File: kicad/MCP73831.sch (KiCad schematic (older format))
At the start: 13 parts, among them J1 BATT, U2 MCP73831-2-OT

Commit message: improve kicad
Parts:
- added TP1: TestPoint_2Pole, TestPoint:TestPoint_2Pads_Pitch2.54mm_Drill0.8mm, symbol Connector:TestPoint_2Pole
- R6: value 1M -> 270k
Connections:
- net GND: now also TP1.2
- net VOUT: now also TP1.1
- net VBAT: now reaches C2.1, D1.2 (S), J1.2 (Pin_2), R5.1, U2.3 (VBAT)
- net STAT renamed V_STATUS
- net VOLT renamed V_PROBE
- no-connect marks 1 -> 0
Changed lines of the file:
@@
 Text HLabel 4250 2500 0    50   Input ~ 0
 VIN
-Text HLabel 8850 2700 2    50   Input ~ 0
+Text HLabel 8850 2700 2    50   Output ~ 0
 VOUT
 Wire Wire Line
@@
 	6200 3700 6200 3800
 Text HLabel 6100 3350 0    50   Input ~ 0
-STAT
+V_STATUS
 Wire Wire Line
 	6100 3350 6200 3350
@@
 P 7550 3300
 F 0 "R6" H 7620 3346 50  0000 L CNN
-F 1 "1M" H 7620 3255 50  0000 L CNN
+F 1 "270k" H 7620 3255 50  0000 L CNN
 F 2 "Resistor_SMD:R_0805_2012Metric_Pad1.15x1.40mm_HandSolder" V 7480 3300 50  0001 C CNN
 F 3 "~" H 7550 3300 50  0001 C CNN
@@
 	1    0    0    -1
 $EndComp
-Text HLabel 8050 3100 2    50   Input ~ 0
-VOLT
+Text HLabel 8050 3100 2    50   Output ~ 0
+V_PROBE
 Wire Wire Line
 	6100 2700 6650 2700
@@
 $EndComp
 Wire Wire Line
-	6650 2700 7100 2700
+	6650 2700 6850 2700
 Connection ~ 6650 2700
 Wire Wire Line
@@
 	7700 2350 7950 2350
 Connection ~ 7950 2350
-NoConn ~ 7250 2750
+$Comp
+L Connector:TestPoint_2Pole TP1
+U 1 1 5C3B9527
+P 8500 2900
+F 0 "TP1" V 8454 2958 50  0000 L CNN
+F 1 "TestPoint_2Pole" V 8545 2958 50  0000 L CNN
+F 2 "TestPoint:TestPoint_2Pads_Pitch2.54mm_Drill0.8mm" H 8500 2900 50  0001 C CNN
+F 3 "~" H 8500 2900 50  0001 C CNN
+	1    8500 2900
+	0    1    1    0
+$EndComp
+$Comp
+L power:GND #PWR0121
+U 1 1 5C3B95F4
+P 8500 3200
+F 0 "#PWR0121" H 8500 2950 50  0001 C CNN
+F 1 "GND" H 8505 3027 50  0000 C CNN
+F 2 "" H 8500 3200 50  0001 C CNN
+F 3 "" H 8500 3200 50  0001 C CNN
+	1    8500 3200
+	1    0    0    -1
+$EndComp
+Wire Wire Line
+	8500 3100 8500 3200
+Text HLabel 6950 2500 2    50   Output ~ 0
+VBAT
+Wire Wire Line
+	6850 2700 6850 2500
+Wire Wire Line
+	6850 2500 6950 2500
+Connection ~ 6850 2700
+Wire Wire Line
+	6850 2700 7100 2700
 $EndSCHEMATC

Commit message: updates
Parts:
- D1: symbol DMP1045U:DMP1045U -> esp8266-rescue:DMP1045U-DMP1045U
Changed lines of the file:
@@
 $Descr A4 11693 8268
 encoding utf-8
-Sheet 2 3
+Sheet 2 4
 Title ""
 Date ""
@@
 	7100 3000 7100 3150
 $Comp
-L DMP1045U:DMP1045U D1
+L esp8266-rescue:DMP1045U-DMP1045U D1
 U 1 1 5C39EFFF
 P 8050 2700

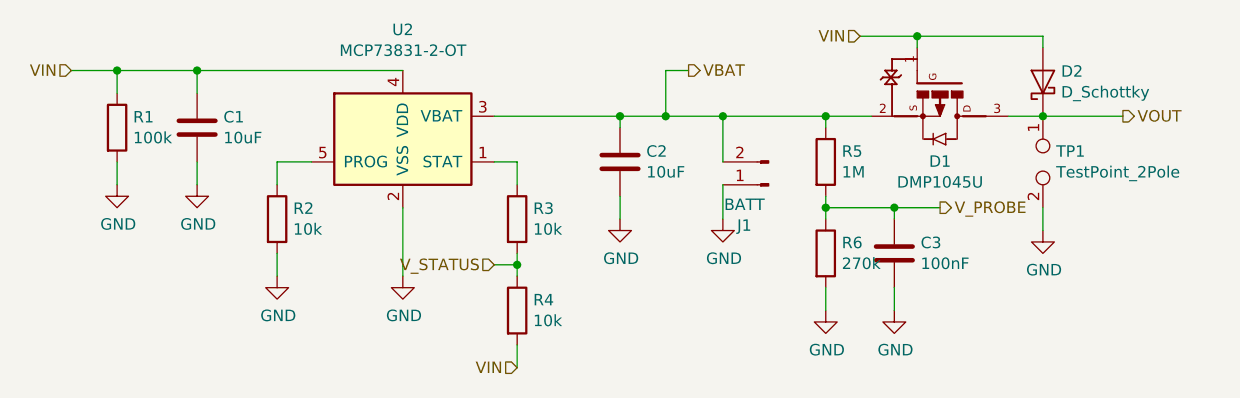
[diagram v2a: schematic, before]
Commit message: add 18B20 on board
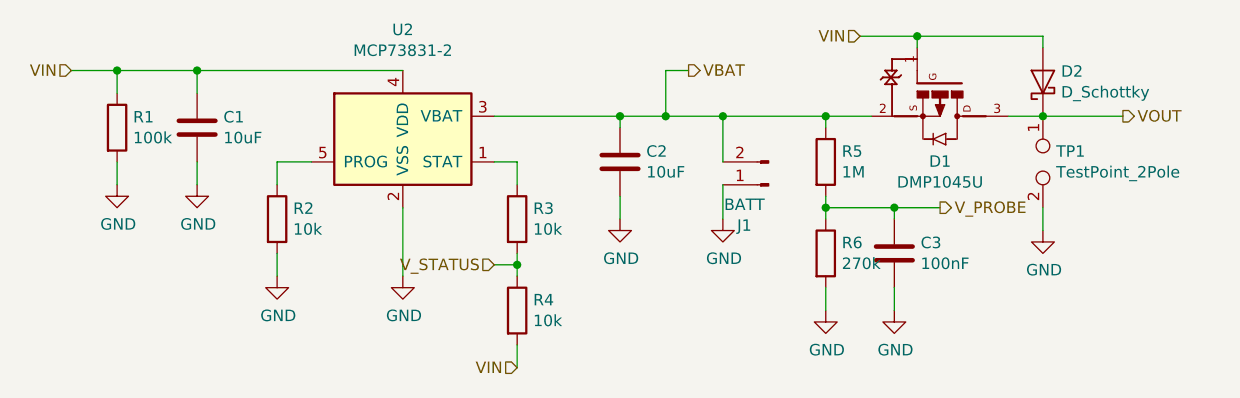
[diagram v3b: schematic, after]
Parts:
- U2: value MCP73831-2-OT -> MCP73831-2
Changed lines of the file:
@@
 P 5700 2800
 F 0 "U2" H 5700 3278 50  0000 C CNN
-F 1 "MCP73831-2-OT" H 5700 3187 50  0000 C CNN
+F 1 "MCP73831-2" H 5700 3187 50  0000 C CNN
 F 2 "Package_TO_SOT_SMD:SOT-23-5" H 5750 2550 50  0001 L CIN
 F 3 "http://ww1.microchip.com/downloads/en/DeviceDoc/20001984g.pdf" H 5550 2750 50  0001 C CNN

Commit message: correst bsp75 footprint
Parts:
- C1: footprint Capacitor_SMD:C_0805_2012Metric_Pad1.15x1.40mm_HandSolder -> Connector_Wire:SolderWirePad_1x01_SMD_5x10mm
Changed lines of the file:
@@
 F 0 "C1" H 4915 2796 50  0000 L CNN
 F 1 "10uF" H 4915 2705 50  0000 L CNN
-F 2 "Capacitor_SMD:C_0805_2012Metric_Pad1.15x1.40mm_HandSolder" H 4838 2600 50  0001 C CNN
+F 2 "Connector_Wire:SolderWirePad_1x01_SMD_5x10mm" H 4838 2600 50  0001 C CNN
 F 3 "~" H 4800 2750 50  0001 C CNN
 	1    4800 2750

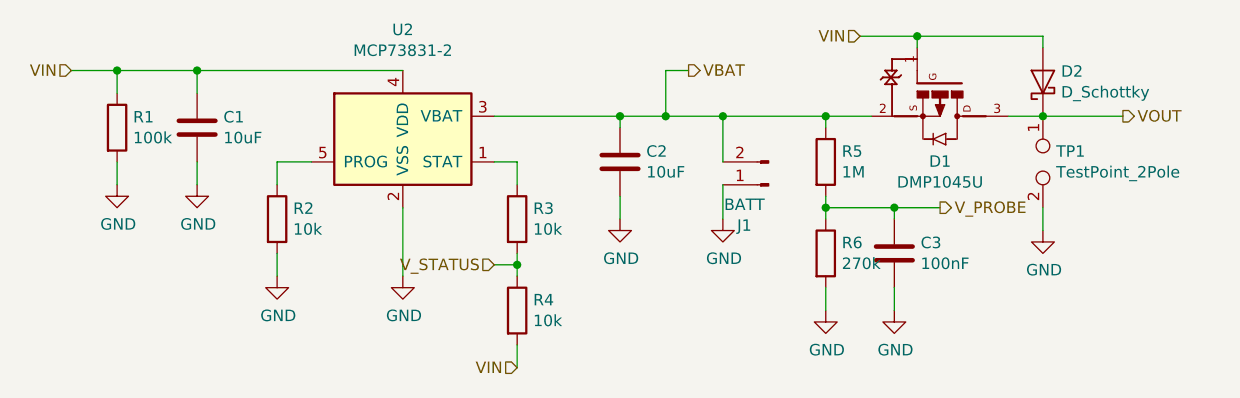
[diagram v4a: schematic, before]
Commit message: add test points in kicad
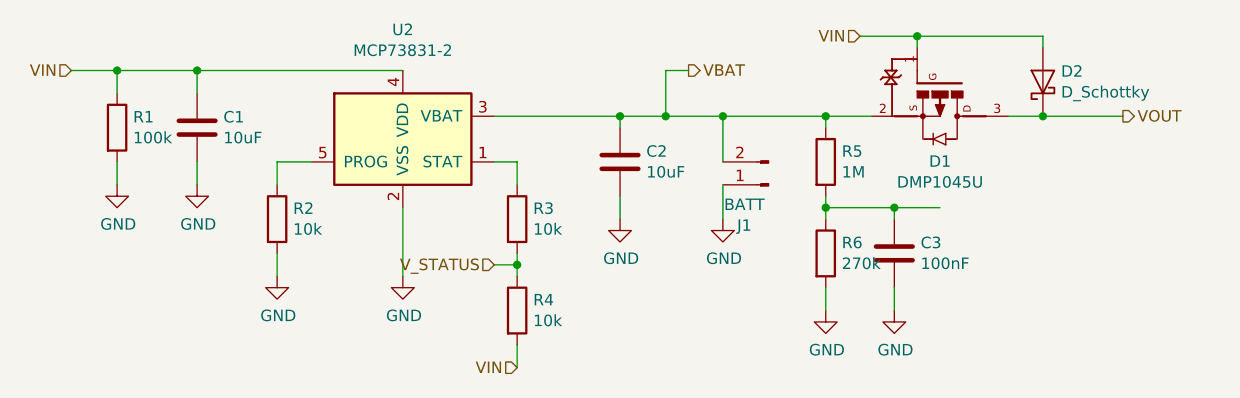
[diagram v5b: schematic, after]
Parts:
- removed TP1: TestPoint_2Pole, TestPoint:TestPoint_2Pads_Pitch2.54mm_Drill0.8mm, symbol Connector:TestPoint_2Pole
- C1: footprint Connector_Wire:SolderWirePad_1x01_SMD_5x10mm -> Capacitor_SMD:C_0805_2012Metric_Pad1.15x1.40mm_HandSolder
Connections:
- net V_PROBE: no longer names the net of C3.1, R5.2, R6.1
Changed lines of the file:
@@
 	1    0    0    -1
 $EndComp
-Text HLabel 8050 3100 2    50   Output ~ 0
-V_PROBE
 Wire Wire Line
 	6100 2700 6650 2700
@@
 F 0 "C1" H 4915 2796 50  0000 L CNN
 F 1 "10uF" H 4915 2705 50  0000 L CNN
-F 2 "Connector_Wire:SolderWirePad_1x01_SMD_5x10mm" H 4838 2600 50  0001 C CNN
+F 2 "Capacitor_SMD:C_0805_2012Metric_Pad1.15x1.40mm_HandSolder" H 4838 2600 50  0001 C CNN
 F 3 "~" H 4800 2750 50  0001 C CNN
 	1    4800 2750
@@
 	7700 2350 7950 2350
 Connection ~ 7950 2350
-$Comp
-L Connector:TestPoint_2Pole TP1
-U 1 1 5C3B9527
-P 8500 2900
-F 0 "TP1" V 8454 2958 50  0000 L CNN
-F 1 "TestPoint_2Pole" V 8545 2958 50  0000 L CNN
-F 2 "TestPoint:TestPoint_2Pads_Pitch2.54mm_Drill0.8mm" H 8500 2900 50  0001 C CNN
-F 3 "~" H 8500 2900 50  0001 C CNN
-	1    8500 2900
-	0    1    1    0
-$EndComp
-$Comp
-L power:GND #PWR0121
-U 1 1 5C3B95F4
-P 8500 3200
-F 0 "#PWR0121" H 8500 2950 50  0001 C CNN
-F 1 "GND" H 8505 3027 50  0000 C CNN
-F 2 "" H 8500 3200 50  0001 C CNN
-F 3 "" H 8500 3200 50  0001 C CNN
-	1    8500 3200
-	1    0    0    -1
-$EndComp
-Wire Wire Line
-	8500 3100 8500 3200
 Text HLabel 6950 2500 2    50   Output ~ 0
 VBAT

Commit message: working on routing
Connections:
- net V_PROBE: now reaches C3.1, R5.2, R6.1
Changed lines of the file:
@@
 Wire Wire Line
 	6850 2700 7100 2700
+Text HLabel 8050 3100 2    50   Output ~ 0
+V_PROBE
 $EndSCHEMATC
